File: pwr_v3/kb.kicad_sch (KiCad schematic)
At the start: 15 parts, among them J1 Conn_01x12, Q2 BSS84

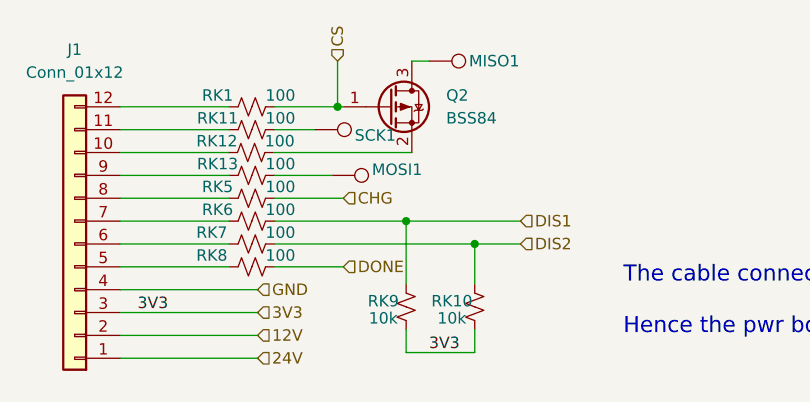
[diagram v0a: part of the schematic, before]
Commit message: Schematic and layout updated
Sch - Unwanted global labels removed from IMU, added new kicker labels, changed kicker connector footprint.
Layout - Updated kicker and encoder positions, routing updated.
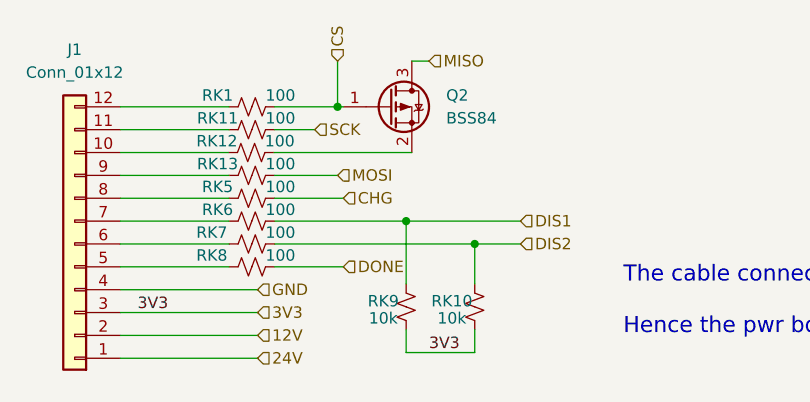
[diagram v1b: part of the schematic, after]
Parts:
- removed MISO1, MOSI1, SCK1: TestPoint, TestPoint:TestPoint_Pad_3.0x3.0mm, symbol Connector:TestPoint
- J1: footprint CON12_1X12_UR_DF13:CON12_1X12_UR_DF13 -> 530471210_12p:530471210
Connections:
- net MOSI: now reaches RK13.2
- net MISO: now reaches Q2.3 (D)
- net SCK: now reaches RK11.2

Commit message: Finalized files
Final files used for fabrication. Docs and Images added for easy view.
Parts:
- J1: now left out of the parts list
